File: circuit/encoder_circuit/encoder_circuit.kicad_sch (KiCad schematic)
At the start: 6 parts, among them J1 Conn_01x04

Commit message: 整理
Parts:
- U1: footprint mylib:NJL5820R -> OptoDevice:NJL5820R
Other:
- moved on the sheet: C1, J1, R1, R2, R3, U1

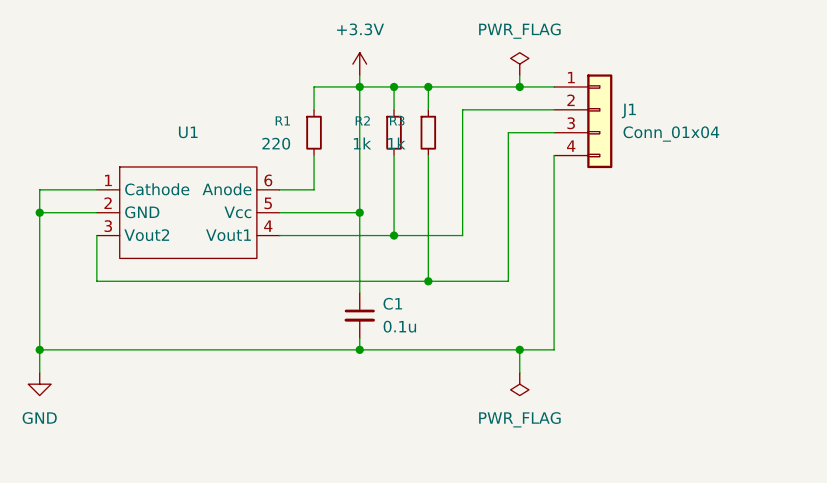
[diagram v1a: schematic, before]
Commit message: エンコーダ基板の回路図更新
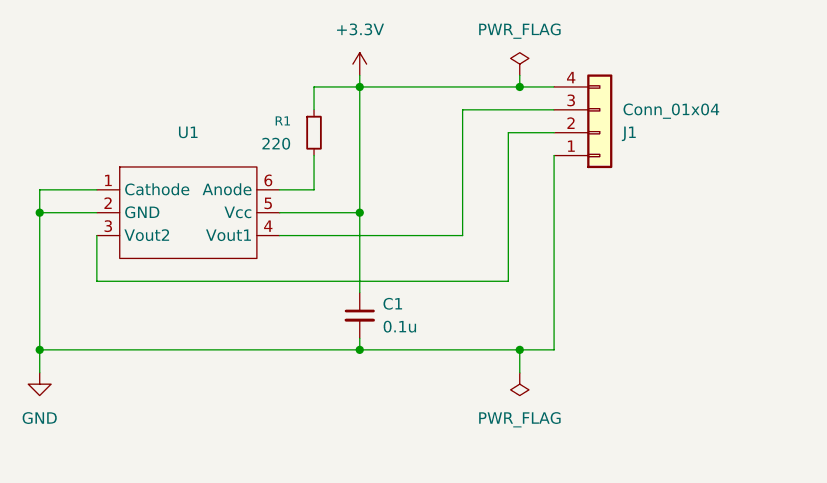
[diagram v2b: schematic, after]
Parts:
- removed R2, R3: 1k, Resistor_SMD:R_0603_1608Metric_Pad0.98x0.95mm_HandSolder, symbol Device:R_Small
- J1: footprint Connector_PinHeader_2.54mm:PinHeader_1x04_P2.54mm_Vertical -> Connector_JST:JST_PH_B4B-PH-K_1x04_P2.00mm_Vertical
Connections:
- net +3.3V: now also J1.4 (Pin_4); no longer J1.1 (Pin_1)
- net GND: now also J1.1 (Pin_1); no longer J1.4 (Pin_4)
- net at U1.3 (Vout2): now also J1.2 (Pin_2); no longer J1.3 (Pin_3)
- net at U1.4 (Vout1): now also J1.3 (Pin_3); no longer J1.2 (Pin_2)

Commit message: エンコーダ基板修正
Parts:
- J1: value Conn_01x04 -> PH
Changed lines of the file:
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@@
 			)
 		)
-		(property "Value" "Conn_01x04"
+		(property "Value" "PH"
 			(at 187.96 80.0101 0)
 			(effects
